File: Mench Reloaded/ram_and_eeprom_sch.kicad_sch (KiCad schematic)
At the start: 23 parts, among them J1 DC Power, J1 XBUS_265, J2 P4x, J3 P5x, J3 RAM CSB select, J4 P6x, J5 TGx, J7 FTDI serial, U1 LM7805_TO220, U2 128K RAM, U3 28C256, U5 74HC00

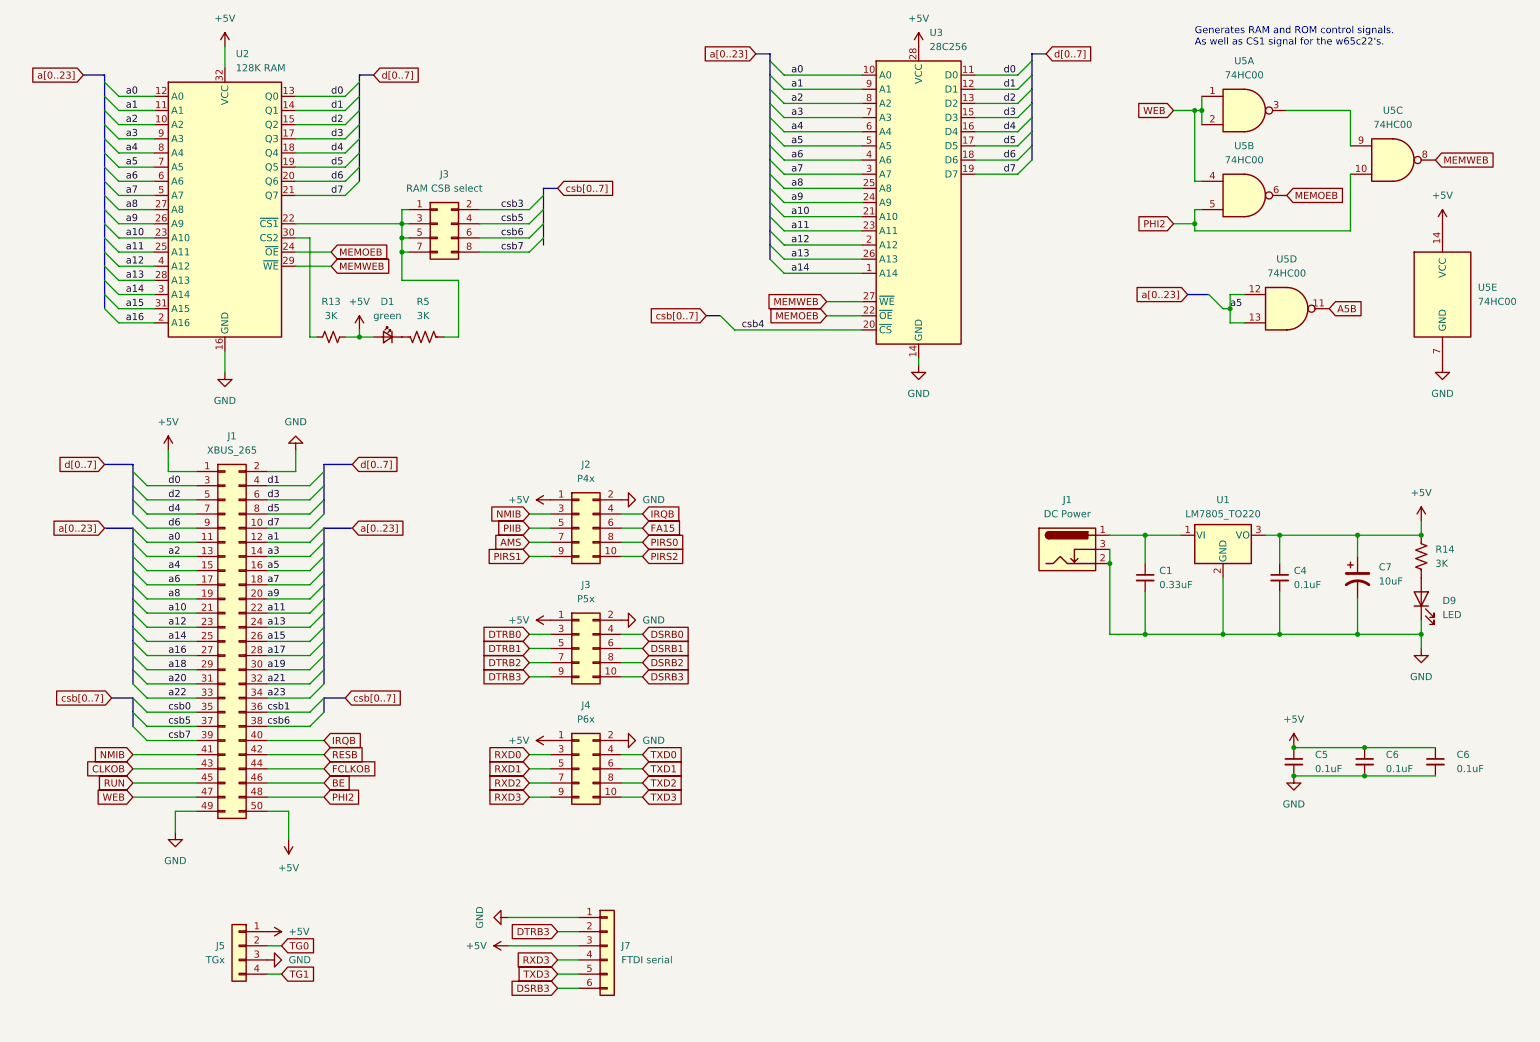
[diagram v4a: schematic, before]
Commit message: Reworked the schematic to aid with routing. Began routing the pcb.
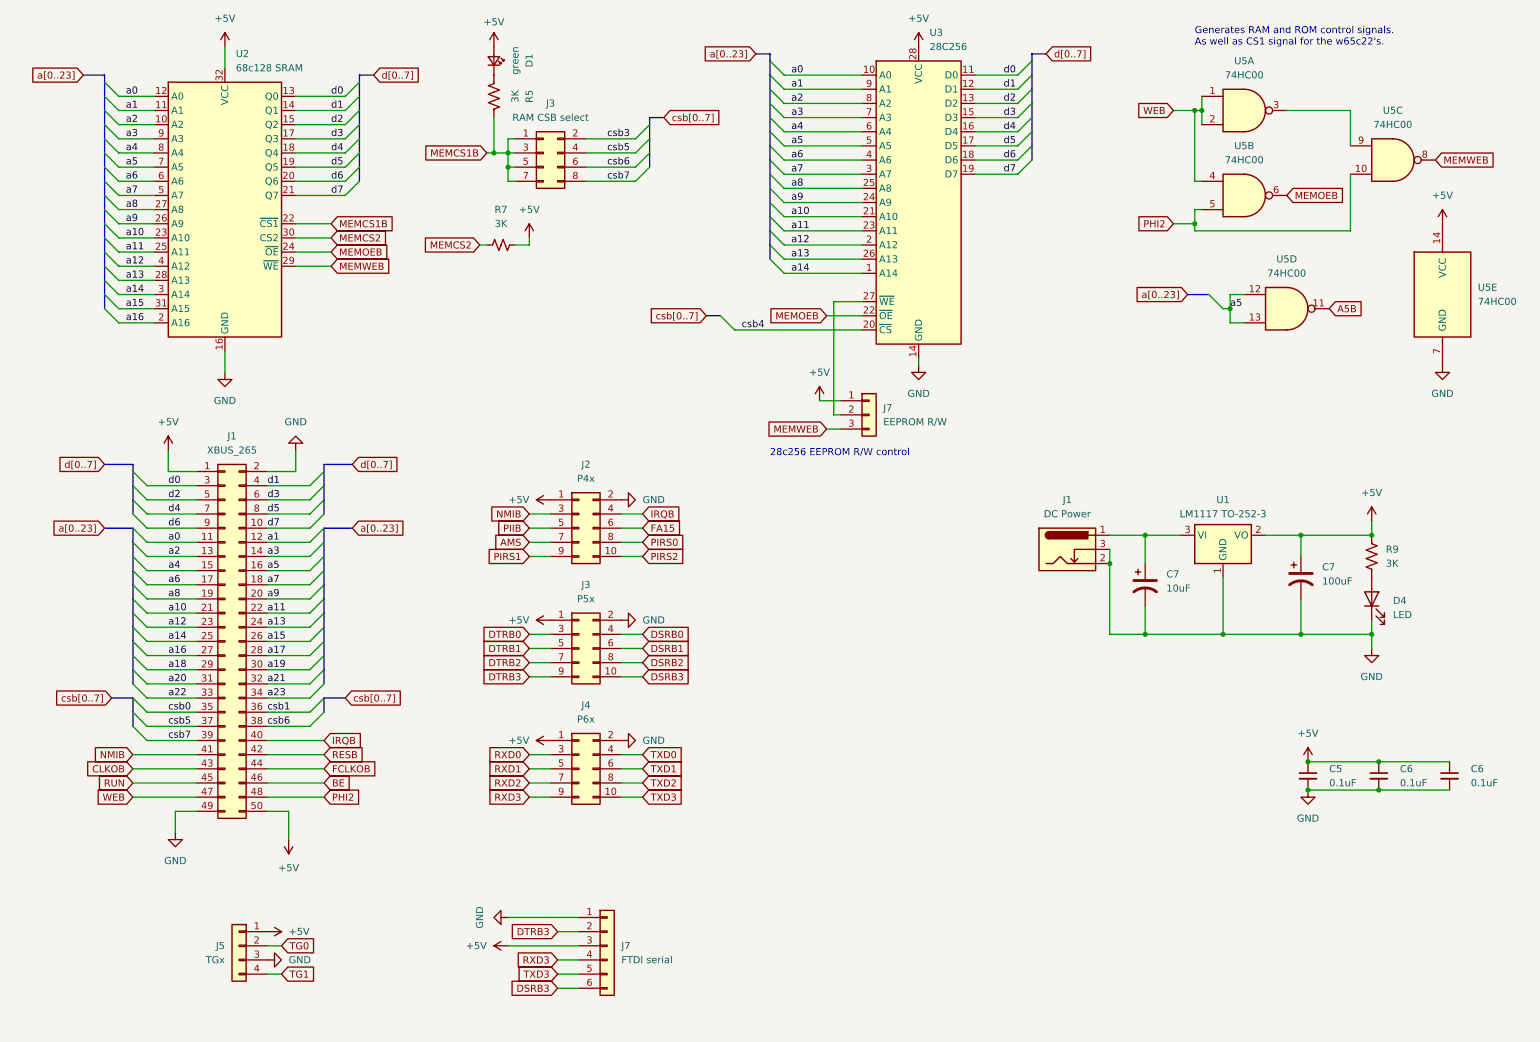
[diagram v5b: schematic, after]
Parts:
- removed C1: 0.33uF, Capacitor_SMD:C_0805_2012Metric_Pad1.18x1.45mm_HandSolder, symbol Device:C_Small
- removed C4: 0.1uF, Capacitor_SMD:C_0805_2012Metric_Pad1.18x1.45mm_HandSolder, symbol Device:C_Small
- removed R13: 3K, Resistor_SMD:R_0805_2012Metric_Pad1.20x1.40mm_HandSolder, symbol Device:R_Small_US
- added C7: 10uF, Capacitor_THT:CP_Radial_D5.0mm_P2.50mm, symbol Device:C_Polarized_US
- added J7: EEPROM R/W, Connector_PinHeader_2.54mm:PinHeader_1x03_P2.54mm_Vertical, symbol Connector_Generic:Conn_01x03
- added R7: 3K, Resistor_SMD:R_0805_2012Metric_Pad1.20x1.40mm_HandSolder, symbol Device:R_Small_US
- C7: value 10uF -> 100uF
- U1: value LM7805_TO220 -> LM1117 TO-252-3; footprint Package_TO_SOT_THT:TO-220-3_Horizontal_TabDown -> Package_TO_SOT_SMD:TO-252-3_TabPin2; symbol Regulator_Linear:LM7805_TO220 -> Regulator_Linear:LM1117DT-5.0
- U2: value 128K RAM -> 68c128 SRAM; footprint Package_DIP:DIP-32_W15.24mm_Socket_LongPads -> Package_DIP:DIP-32_W15.24mm_Socket
- U3: footprint Package_DIP:DIP-28_W15.24mm_Socket_LongPads -> Package_DIP:DIP-28_W15.24mm_Socket
- renumbered D9 to D4, R14 to R9
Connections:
- net +5V: now also U1.2 (VO), J7.1 (Pin_1), R7.1; no longer U1.3 (VO)
- net GND: now also U1.1 (GND), C7.2; no longer U1.2 (GND)
- net MEMWEB: now also J7.3 (Pin_3); no longer U3.27 (~{WE})
- net MEMCS2: now reaches U2.30 (CS2)
- net MEMCS2: now also R7.2
- net MEMCS1B: now reaches J3.1 (Pin_1), J3.3 (Pin_3), J3.5 (Pin_5), J3.7 (Pin_7), R5.1, U2.22 (~{CS1})
- net at J1.1: now also U1.3 (VI), C7.1; no longer U1.1 (VI)
- new net: J7.2 (Pin_2), U3.27 (~{WE})
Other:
- note added: "28c256 EEPROM R/W control"
- moved on the sheet: C5, C6, C7, D4, R9

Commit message: Completed all traces. Added a Zif socket footprint to ensure one will fit. Added a solder jumper for RAM options.
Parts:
- added JP1: 68c256 Jumper, Jumper:SolderJumper-2_P1.3mm_Open_Pad1.0x1.5mm, symbol Jumper:SolderJumper_2_Open
- renumbered C7 to C10, C5 to C11, C6 to C12, C6 to C13, C7 to C9, D1 to D3, J5 to J2, J2 to J4, J3 to J5, J4 to J6, J7 to J8, J1 to J9, R5 to R8, U1 to U4
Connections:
- net GND: now also U5.12, U5.13
- net a17: now also JP1.1 (A)
- net a5: no longer U5.12, U5.13
- net A5B: no longer names the net of U5.11
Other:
- note added: "Inputs tied low to avoid floating output."

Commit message: Added power selector header (ftdi vs battery). Added 128kB vs 256kB RAM selector. Added pull up for RESB and DS1813. Reworked traces at top of the board using streets and avenues.
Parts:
- removed JP1: 68c256 Jumper, Jumper:SolderJumper-2_P1.3mm_Open_Pad1.0x1.5mm, symbol Jumper:SolderJumper_2_Open
- added J11: Power Sel, Connector_PinHeader_2.54mm:PinHeader_1x03_P2.54mm_Vertical, symbol Connector_Generic:Conn_01x03
- added J7: 68c256 Sel, Connector_PinHeader_2.54mm:PinHeader_1x02_P2.54mm_Vertical, symbol Connector_Generic:Conn_01x02
- D3: value green -> LED
- renumbered J7 to J10, J9 to J8, J8 to J9, R9 to R10, R7 to R9
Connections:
- net +5V: now also J11.2 (Pin_2); no longer C10.1, J10.3 (Pin_3), U4.2 (VO)
- net a17: now also J7.1 (Pin_1)
- new net: J10.3 (Pin_3), J11.1 (Pin_1)
- new net: C10.1, J11.3 (Pin_3), U4.2 (VO)
- new net a17_Select: J7.2 (Pin_2)
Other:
- moved on the sheet: C10, C11, C12, C13, C9, D4, J1, J10, J8, R10, U4

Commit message: Moved EEPROM North to create more space for traces. Reworked all traces from CPU to fix rats nest wiring. Added LED to csb2 to allow for debugging when internal bus is used. Added to list of signal net classes to make consistant data traces.
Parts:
- renumbered D3 to D4, D4 to D5, R9 to R10, R10 to R11, R8 to R9
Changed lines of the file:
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@@
 		(dnp no)
 		(fields_autoplaced yes)
-		(property "Reference" "R8"
+		(property "Reference" "R9"
 			(at 105.41 29.21 90)
 			(effects
@@
 			(project "Mench Reloaded"
 				(path "/e63e39d7-6ac0-4ffd-8aa3-1841a4541b55/65831a0a-ff7e-4102-95d5-98ddaae72b40"
-					(reference "R8")
+					(reference "R9")
 					(unit 1)
 				)
@@
 		(on_board yes)
 		(dnp no)
-		(property "Reference" "D3"
+		(property "Reference" "D4"
 			(at 105.41 22.7965 0)
 			(effects
@@
 			(project "Mench Reloaded"
 				(path "/e63e39d7-6ac0-4ffd-8aa3-1841a4541b55/65831a0a-ff7e-4102-95d5-98ddaae72b40"
-					(reference "D3")
+					(reference "D4")
 					(unit 1)
 				)
@@
 		(dnp no)
 		(fields_autoplaced yes)
-		(property "Reference" "D4"
+		(property "Reference" "D5"
 			(at 237.49 148.9075 90)
 			(effects
@@
 			(project "Mench Reloaded"
 				(path "/e63e39d7-6ac0-4ffd-8aa3-1841a4541b55/65831a0a-ff7e-4102-95d5-98ddaae72b40"
-					(reference "D4")
+					(reference "D5")
 					(unit 1)
 				)
@@
 		(dnp no)
 		(fields_autoplaced yes)
-		(property "Reference" "R10"
+		(property "Reference" "R11"
 			(at 236.22 139.7 0)
 			(effects
@@
 			(project "Mench Reloaded"
 				(path "/e63e39d7-6ac0-4ffd-8aa3-1841a4541b55/65831a0a-ff7e-4102-95d5-98ddaae72b40"
-					(reference "R10")
+					(reference "R11")
 					(unit 1)
 				)
@@
 		(dnp no)
 		(fields_autoplaced yes)
-		(property "Reference" "R9"
+		(property "Reference" "R10"
 			(at 100.33 49.53 90)
 			(effects
@@
 			(project "Mench Reloaded"
 				(path "/e63e39d7-6ac0-4ffd-8aa3-1841a4541b55/65831a0a-ff7e-4102-95d5-98ddaae72b40"
-					(reference "R9")
-					(unit 1)
-				)
+					(reference "R10")
+					(unit 1)
+				)
